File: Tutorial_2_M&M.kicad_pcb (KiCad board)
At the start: 2 copper layers, 40 x 20 mm, 7 parts, among them J1 USB_C_Receptacle_USB2.0_16P, J2 Conn_01x06, U2 AZ1117-3.3

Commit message: PCB layout completed
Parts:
- moved R1 4.19 mm to (160.2, 88.0), turned to 0 degrees
- moved R2 1.75 mm to (158.8, 82.2), turned to 0 degrees
- moved C2 1.38 mm to (175.4, 87.0), turned to 0 degrees
- moved C1 1.10 mm to (163.4, 87.4)
- moved J2 0.94 mm to (185.3, 86.1), turned to 180 degrees
- moved J1 0.11 mm to (152.1, 87.0)
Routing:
- net USB_D+: track 0.00 -> 39.1 mm
- net VBUS: track 0.00 -> 33.7 mm
- net USB_D-: track 0.00 -> 33.6 mm
- net GND: track 4.31 -> 29.8 mm, vias 1 -> 7
- net +3.3V: track 0.00 -> 21.2 mm
- net Net-(J1-CC1): track 0.00 -> 4.91 mm
- net Net-(J1-CC2): track 0.00 -> 3.90 mm
- removed copper zone on F.Cu, net GND

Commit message: Pictures added
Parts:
- added G***: LOGO, demo.preety:logo_HSRW, F.Cu at (161.4, 94.0)
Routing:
- net VBUS: track 33.7 -> 40.3 mm
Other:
- board text added: "33615"
- board text added: "Vasile Vataman"
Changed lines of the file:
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@@
 		)
 		(property "Value" "USB_C_Receptacle_USB2.0_16P"
-			(at 0 5 270)
+			(at 0 5.91 270)
 			(unlocked yes)
 			(layer "F.Fab")
@@
 		)
 	)
+	(footprint "demo.preety:logo_HSRW"
+		(layer "F.Cu")
+		(at 161.4 94)
+		(property "Reference" "G***"
+			(at 0 0 0)
+			(layer "F.SilkS")
+			(hide yes)
+			(effects
+				(font
+					(size 1.5 1.5)
+					(thickness 0.3)
+				)
+			)
+		)
+		(property "Value" "LOGO"
+			(at 0.75 0 0)
+			(layer "F.SilkS")
+			(hide yes)
+			(effects
+				(font
+					(size 1.5 1.5)
+					(thickness 0.3)
+				)
+			)
+		)
+		(property "Datasheet" ""
+			(at 0 0 0)
+			(layer "F.Fab")
+			(hide yes)
+			(effects
+				(font
+					(size 1.27 1.27)
+					(thickness 0.15)
+				)
+			)
+		)
+		(property "Description" ""
+			(at 0 0 0)
+			(layer "F.Fab")
+			(hide yes)
+			(effects
+				(font
+					(size 1.27 1.27)
+					(thickness 0.15)
+				)
+			)
+		)
+		(attr board_only exclude_from_pos_files exclude_from_bom)
+		(fp_poly
+			(pts
+				(xy -1.027889 -2.230584) (xy -0.958511 -2.206683) (xy -0.947217 -2.200501) (xy -0.936674 -2.194156)
+				(xy -0.926341 -2.187179) (xy -0.915155 -2.178304) (xy -0.902049 -2.166266) (xy -0.885958 -2.149801)
+				(xy -0.865817 -2.127643) (xy -0.84056 -2.098529) (xy -0.809122 -2.061194) (xy -0.770437 -2.014372)
+				(xy -0.723441 -1.9568) (xy -0.667067 -1.887211) (xy -0.60025 -1.804343) (xy -0.521925 -1.70693)
+				(xy -0.431026 -1.593707) (xy -0.330784 -1.468765) (xy -0.046886 -1.114871) (xy -0.047143 0.019837)
+				(xy -0.047195 0.208213) (xy -0.047279 0.374587) (xy -0.047424 0.5204) (xy -0.047661 0.647092) (xy -0.048017 0.756104)
+				(xy -0.048523 0.848877) (xy -0.049207 0.926851) (xy -0.0501 0.991466) (xy -0.05123 1.044164) (xy -0.052626 1.086385)
+				(xy -0.054318 1.11957) (xy -0.056335 1.145159) (xy -0.058706 1.164593) (xy -0.061461 1.179312) (xy -0.064629 1.190757)
+				(xy -0.068239 1.20037) (xy -0.071276 1.207291) (xy -0.111601 1.274865) (xy -0.165512 1.32563) (xy -0.216844 1.355175)
+				(xy -0.291674 1.378186) (xy -0.370986 1.380734) (xy -0.438054 1.365901) (xy -0.50593 1.329881) (xy -0.563407 1.275921)
+				(xy -0.597733 1.223944) (xy -0.627089 1.166909) (xy -0.630268 0.130026) (xy -0.633447 -0.906857)
+				(xy -0.978099 -1.33623) (xy -1.048844 -1.424601) (xy -1.115769 -1.508655) (xy -1.177288 -1.586367)
+				(xy -1.231818 -1.655717) (xy -1.277775 -1.714682) (xy -1.313573 -1.761241) (xy -1.33763 -1.793371)
+				(xy -1.347852 -1.808143) (xy -1.369782 -1.863386) (xy -1.380227 -1.93002) (xy -1.378228 -1.99849)
+				(xy -1.370716 -2.036268) (xy -1.345407 -2.09129) (xy -1.303716 -2.144715) (xy -1.252105 -2.190068)
+				(xy -1.197036 -2.220877) (xy -1.181117 -2.226229) (xy -1.104788 -2.237396)
+			)
+			(stroke
+				(width 0)
+				(type solid)
+			)
+			(fill yes)
+			(layer "F.SilkS")
+		)
+		(fp_poly
+			(pts
+				(xy 1.376176 -2.286056) (xy 1.376269 -2.253744) (xy 1.376242 -2.202875) (xy 1.3761 -2.135894) (xy 1.375848 -2.055245)
+				(xy 1.375492 -1.963369) (xy 1.375039 -1.862711) (xy 1.374798 -1.813868) (xy 1.372347 -1.330365)
+				(xy 1.032574 -0.879096) (xy 0.692801 -0.427827) (xy 0.685302 0.814628) (xy 0.683996 1.013242) (xy 0.68256 1.198577)
+				(xy 0.681011 1.369622) (xy 0.679362 1.525366) (xy 0.677629 1.664799) (xy 0.675827 1.786909) (xy 0.67397 1.890687)
+				(xy 0.672075 1.975121) (xy 0.670155 2.0392) (xy 0.668226 2.081915) (xy 0.666302 2.102253) (xy 0.666197 2.102702)
+				(xy 0.647021 2.144091) (xy 0.612704 2.189094) (xy 0.569419 2.231564) (xy 0.523337 2.265354) (xy 0.485073 2.283115)
+				(xy 0.406109 2.295848) (xy 0.327337 2.289216) (xy 0.284125 2.27622) (xy 0.227541 2.244276) (xy 0.174433 2.197921)
+				(xy 0.134139 2.145443) (xy 0.13149 2.140758) (xy 0.128407 2.133909) (xy 0.125645 2.124389) (xy 0.123183 2.110917)
+				(xy 0.121001 2.092212) (xy 0.119077 2.066993) (xy 0.11739 2.033978) (xy 0.115917 1.991887) (xy 0.114639 1.939438)
+				(xy 0.113533 1.875351) (xy 0.112578 1.798343) (xy 0.111753 1.707135) (xy 0.111037 1.600445) (xy 0.110408 1.476992)
+				(xy 0.109845 1.335494) (xy 0.109327 1.174672) (xy 0.108832 0.993243) (xy 0.108339 0.789926) (xy 0.108231 0.743483)
+				(xy 0.105111 -0.617001) (xy 0.389542 -0.993152) (xy 0.459398 -1.085552) (xy 0.540099 -1.192325)
+				(xy 0.628368 -1.309133) (xy 0.720927 -1.43164) (xy 0.814499 -1.555507) (xy 0.905807 -1.676396) (xy 0.991573 -1.78997)
+				(xy 1.024317 -1.833337) (xy 1.093198 -1.924537) (xy 1.157644 -2.0098) (xy 1.216306 -2.087347) (xy 1.267836 -2.155397)
+				(xy 1.310886 -2.212173) (xy 1.344108 -2.255895) (xy 1.366153 -2.284784) (xy 1.375675 -2.297062)
+				(xy 1.375955 -2.29737)
+			)
+			(stroke
+				(width 0)
+				(type solid)
+			)
+			(fill yes)
+			(layer "F.SilkS")
+		)
+		(embedded_fonts no)
+	)
 	(gr_rect
 		(start 149 77)
@@
 		(layer "Edge.Cuts")
 	)
+	(gr_text "Vasile Vataman"
+		(at 149.4 96.2 0)
+		(layer "F.SilkS")
+		(effects
+			(font
+				(size 0.9 0.9)
+				(thickness 0.09)
+			)
+			(justify left bottom)
+		)
+	)
+	(gr_text "33615"
+		(at 152.6 94.6 0)
+		(layer "F.SilkS")
+		(effects
+			(font
+				(size 0.9 0.9)
+				(thickness 0.09125)
+			)
+			(justify left bottom)
+		)
+	)
 	(segment
 		(start 186.225 87.775)
@@
 	(via
 		(at 151.035 80.365)
-		(size 0.6)
+		(size 0.8)
 		(drill 0.3)
 		(layers "F.Cu" "B.Cu")
+		(teardrops
+			(best_length_ratio 0.5)
+			(max_length 1)
+			(best_width_ratio 1)
+			(max_width 2)
+			(curved_edges no)
+			(filter_ratio 0.9)
+			(enabled yes)
+			(allow_two_segments yes)
+			(prefer_zone_connections yes)
+		)
 		(net 2)
 	)
 	(via
 		(at 181.4 90)
-		(size 0.6)
+		(size 0.8)
 		(drill 0.3)
 		(layers "F.Cu" "B.Cu")
@@
 	(via
 		(at 163.4 86.6)
-		(size 0.6)
+		(size 0.8)
 		(drill 0.3)
 		(layers "F.Cu" "B.Cu")
@@
 	(via
 		(at 177.6 87)
-		(size 0.6)
+		(size 0.8)
 		(drill 0.3)
 		(layers "F.Cu" "B.Cu")
@@
 	(via
 		(at 151.035 93.4)
-		(size 0.6)
+		(size 0.8)
 		(drill 0.3)
 		(layers "F.Cu" "B.Cu")
@@
 	(via
 		(at 159.625 82.2)
-		(size 0.6)
+		(size 0.8)
 		(drill 0.3)
 		(layers "F.Cu" "B.Cu")
@@
 	(via
 		(at 161.025 88)
-		(size 0.6)
+		(size 0.8)
 		(drill 0.3)
 		(layers "F.Cu" "B.Cu")
@@
 	)
 	(segment
+		(start 154.515 85.300001)
+		(end 154.515 88.58241)
+		(width 0.2)
+		(layer "F.Cu")
+		(net 4)
+	)
+	(segment
 		(start 162.15 89.4)
 		(end 163.4 88.15)
@@
 	)
 	(segment
+		(start 155.18259 89.25)
+		(end 155.94 89.25)
+		(width 0.2)
+		(layer "F.Cu")
+		(net 4)
+	)
+	(segment
+		(start 155.215001 84.6)
+		(end 154.515 85.300001)
+		(width 0.2)
+		(layer "F.Cu")
+		(net 4)
+	)
+	(segment
 		(start 155.94 89.25)
 		(end 155.79 89.4)
@@
 	)
 	(segment
+		(start 154.515 88.58241)
+		(end 155.18259 89.25)
+		(width 0.2)
+		(layer "F.Cu")
+		(net 4)
+	)
+	(segment
 		(start 163.4 88.15)
 		(end 164.7 88.15)
@@
 	)
 	(segment
+		(start 155.79 84.6)
+		(end 155.215001 84.6)
+		(width 0.2)
+		(layer "F.Cu")
+		(net 4)
+	)
+	(segment
 		(start 156.75 88.75)
 		(end 155.79 88.75)
@@
 	)
 	(zone
+		(net 2)
+		(net_name "GND")
+		(layer "F.Cu")
+		(name "$teardrop_padvia$")
+		(hatch none 0.1)
+		(priority 30000)
+		(attr
+			(teardrop
+				(type padvia)
+			)
+		)
+		(connect_pads yes
+			(clearance 0)
+		)
+		(min_thickness 0.0254)
+		(filled_areas_thickness no)
+		(fill yes
+			(thermal_gap 0.5)
+			(thermal_bridge_width 0.5)
+			(island_removal_mode 1)
+			(island_area_min 10)
+		)
+		(polygon
+			(pts
+				(xy 150.935 81.157314) (xy 151.135 81.157314) (xy 151.427314 80.443036) (xy 151.035 80.364) (xy 150.642686 80.443036)
+			)
+		)
+	)
+	(zone

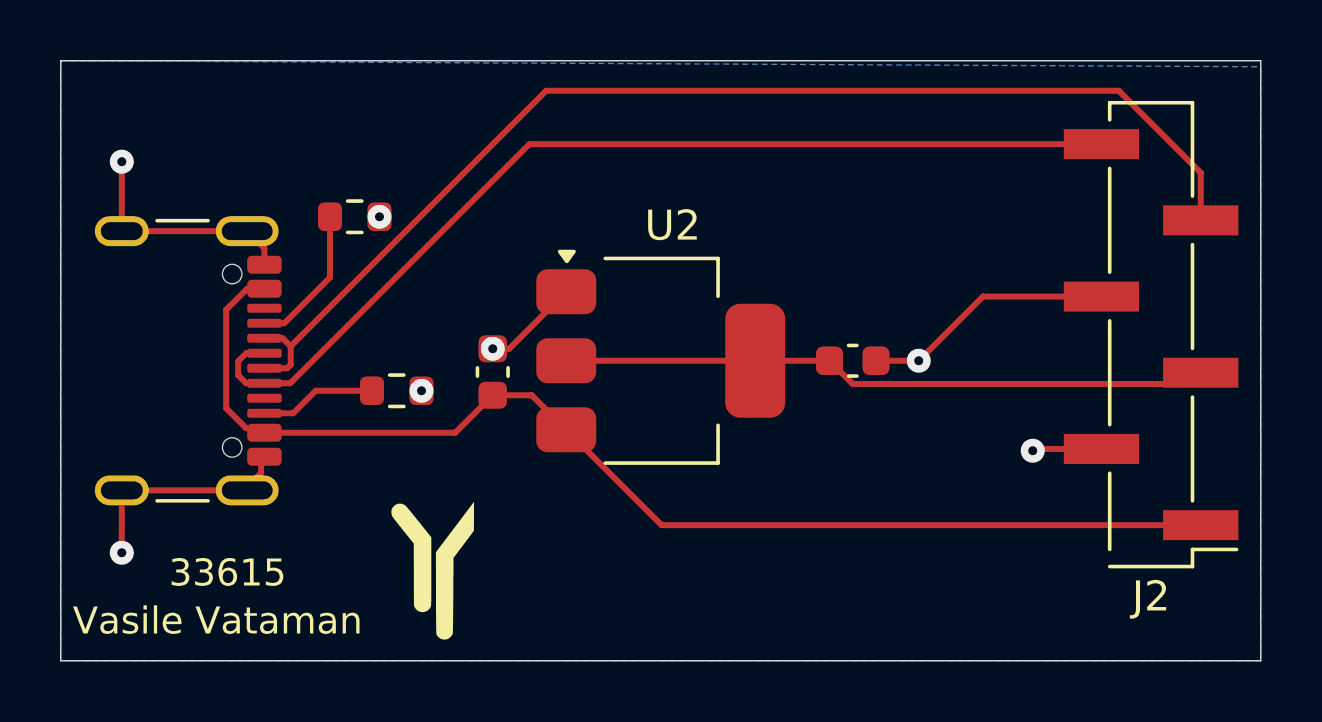
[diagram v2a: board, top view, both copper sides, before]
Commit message: GND Zone added on F.Cu & Gerber Files created
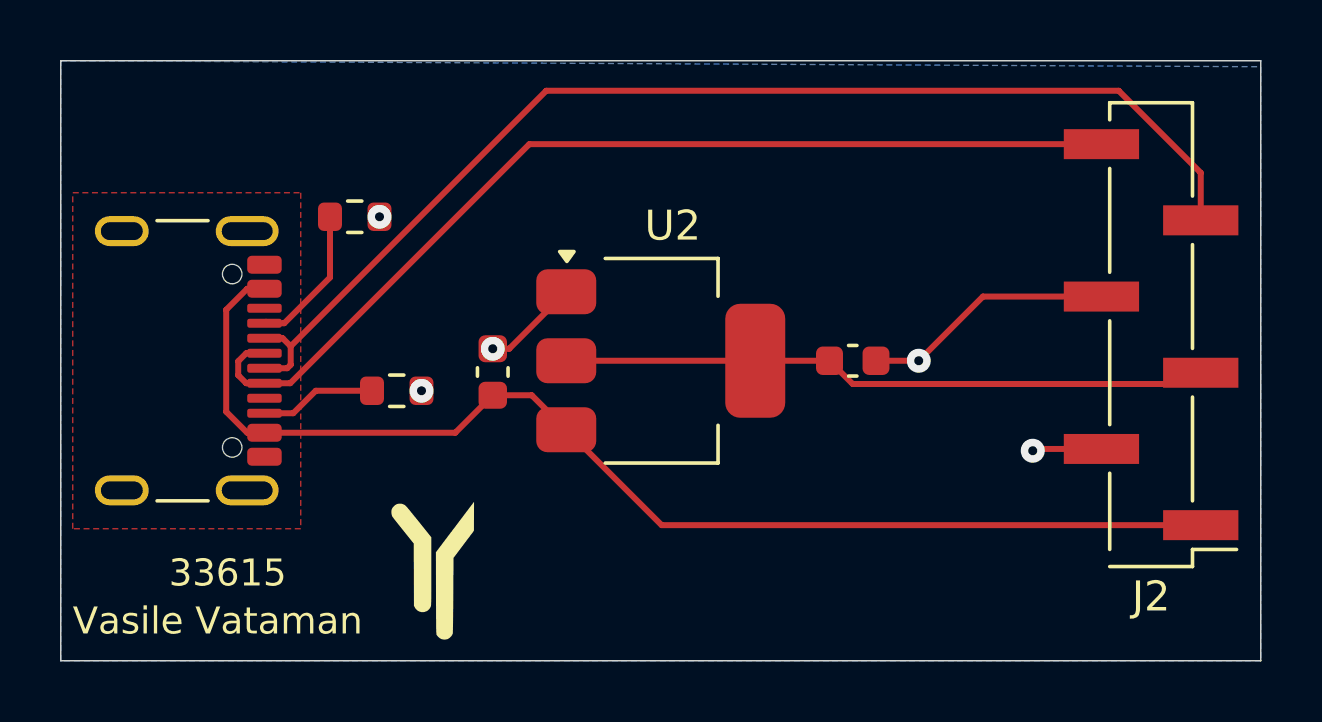
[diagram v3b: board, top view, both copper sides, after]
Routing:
- net GND: track 29.8 -> 14.0 mm, vias 7 -> 5
- added copper zone on F.Cu, net GND
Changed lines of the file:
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@@
 			(outputformat 1)
 			(mirror no)
-			(drillshape 1)
+			(drillshape 0)
 			(scaleselection 1)
-			(outputdirectory "")
+			(outputdirectory "Manufacturing_files/")
 		)
 	)
@@
 	)
 	(segment
-		(start 155.215 91.32)
-		(end 151.035 91.32)
-		(width 0.2)
-		(layer "F.Cu")
-		(net 2)
-	)
-	(segment
-		(start 155.68 90.745)
-		(end 155.105 91.32)
-		(width 0.2)
-		(layer "F.Cu")
-		(net 2)
-	)
-	(segment
-		(start 151.035 82.68)
-		(end 155.215 82.68)
-		(width 0.2)
-		(layer "F.Cu")
-		(net 2)
-	)
-	(segment
-		(start 155.79 83.255)
-		(end 155.215 82.68)
-		(width 0.2)
-		(layer "F.Cu")
-		(net 2)
-	)
-	(segment
 		(start 179.74 84.86)
 		(end 177.6 87)
@@
 	)
 	(segment
-		(start 155.79 83.8)
-		(end 155.79 83.255)
-		(width 0.2)
-		(layer "F.Cu")
-		(net 2)
-	)
-	(segment
-		(start 156.2 83.8)
-		(end 155.79 83.8)
-		(width 0.2)
-		(layer "F.Cu")
-		(net 2)
-	)
-	(segment
-		(start 151.035 80.365)
-		(end 151.035 82.68)
-		(width 0.2)
-		(layer "F.Cu")
-		(net 2)
-	)
-	(segment
 		(start 163.95 86.6)
 		(end 163.4 86.6)
@@
 	)
 	(segment
-		(start 151.035 93.4)
-		(end 151.035 91.32)
-		(width 0.2)
-		(layer "F.Cu")
-		(net 2)
-	)
-	(segment
 		(start 176.175 87)
 		(end 177.6 87)
@@
 		(width 0.2)
 		(layer "F.Cu")
-		(net 2)
-	)
-	(segment
-		(start 155.68 90.2)
-		(end 155.68 90.745)
-		(width 0.2)
-		(layer "F.Cu")
-		(net 2)
-	)
-	(via
-		(at 151.035 80.365)
-		(size 0.8)
-		(drill 0.3)
-		(layers "F.Cu" "B.Cu")
-		(teardrops
-			(best_length_ratio 0.5)
-			(max_length 1)
-			(best_width_ratio 1)
-			(max_width 2)
-			(curved_edges no)
-			(filter_ratio 0.9)
-			(enabled yes)
-			(allow_two_segments yes)
-			(prefer_zone_connections yes)
-		)
 		(net 2)
 	)
@@
 	)
 	(via
-		(at 151.035 93.4)
-		(size 0.8)
-		(drill 0.3)
-		(layers "F.Cu" "B.Cu")
-		(net 2)
-	)
-	(via
 		(at 159.625 82.2)
 		(size 0.8)
@@
 	)
 	(segment
-		(start 154.515 85.300001)
-		(end 154.515 88.58241)
-		(width 0.2)
-		(layer "F.Cu")
-		(net 4)
-	)
-	(segment
 		(start 162.15 89.4)
 		(end 163.4 88.15)
@@
 	)
 	(segment
+		(start 155.79 89.4)
+		(end 155.215001 89.4)
+		(width 0.2)
+		(layer "F.Cu")
+		(net 4)
+	)
+	(segment
 		(start 164.7 88.15)
 		(end 165.85 89.3)
@@
 	)
 	(segment
-		(start 155.18259 89.25)
-		(end 155.94 89.25)
-		(width 0.2)
-		(layer "F.Cu")
-		(net 4)
-	)
-	(segment
-		(start 155.215001 84.6)
+		(start 154.515 88.699999)
 		(end 154.515 85.300001)
 		(width 0.2)
@@
 	)
 	(segment
-		(start 154.515 88.58241)
-		(end 155.18259 89.25)
+		(start 155.215001 84.6)
+		(end 155.79 84.6)
+		(width 0.2)
+		(layer "F.Cu")
+		(net 4)
+	)
+	(segment
+		(start 154.515 85.300001)
+		(end 155.215001 84.6)
+		(width 0.2)
+		(layer "F.Cu")
+		(net 4)
+	)
+	(segment
+		(start 155.215001 89.4)
+		(end 154.515 88.699999)
 		(width 0.2)
 		(layer "F.Cu")
@@
 		(start 163.4 88.15)
 		(end 164.7 88.15)
-		(width 0.2)
-		(layer "F.Cu")
-		(net 4)
-	)
-	(segment
-		(start 155.79 84.6)
-		(end 155.215001 84.6)
 		(width 0.2)
 		(layer "F.Cu")
@@
 		(net_name "GND")
 		(layer "F.Cu")
-		(name "$teardrop_padvia$")
-		(hatch none 0.1)
-		(priority 30000)
-		(attr
-			(teardrop
-				(type padvia)
-			)
-		)
-		(connect_pads yes
-			(clearance 0)
-		)
-		(min_thickness 0.0254)
+		(hatch edge 0.5)
+		(priority 1)
+		(connect_pads
+			(clearance 0.2)
+		)
+		(min_thickness 0.25)
 		(filled_areas_thickness no)
 		(fill yes
-			(thermal_gap 0.5)
-			(thermal_bridge_width 0.5)
-			(island_removal_mode 1)
-			(island_area_min 10)
+			(thermal_gap 0.25)
+			(thermal_bridge_width 0.25)
 		)
 		(polygon
 			(pts
-				(xy 150.935 81.157314) (xy 151.135 81.157314) (xy 151.427314 80.443036) (xy 151.035 80.364) (xy 150.642686 80.443036)
+				(xy 149.4 81.4) (xy 157 81.4) (xy 157 92.6) (xy 149.4 92.6)
 			)
 		)
@@
 		(hatch edge 0.5)
 		(connect_pads
-			(clearance 0.5)
+			(clearance 0.2)
 		)
 		(min_thickness 0.25)
 		(filled_areas_thickness no)
 		(fill yes
-			(thermal_gap 0.5)
-			(thermal_bridge_width 0.5)
+			(thermal_gap 0.25)
+			(thermal_bridge_width 0.25)
 		)
 		(polygon
